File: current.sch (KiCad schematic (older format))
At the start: 42 parts, among them Q401 CJ2302, Q402 CJ2302, Q403 CJ2302, Q404 CJ2302, U401 MAX9919FASA+, U402 MAX9919FASA+, U403 MAX9919FASA+, U404 MAX9919FASA+, U405 MAX9919FASA+

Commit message: significant progress on placement, sch changes for adc routing
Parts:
- R403, R404, R407, R408, R409: footprint Resistors_SMD:R_1206 -> tm-kicad-lib:SMD-0805-R

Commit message: usb refactor on sch and pcb, mechanical constraints on bcp
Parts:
- U401, U402, U403, U404, U405: footprint SMD_Packages:SOIC-8-N -> tm-kicad-lib:SOIC-8-N-1EP

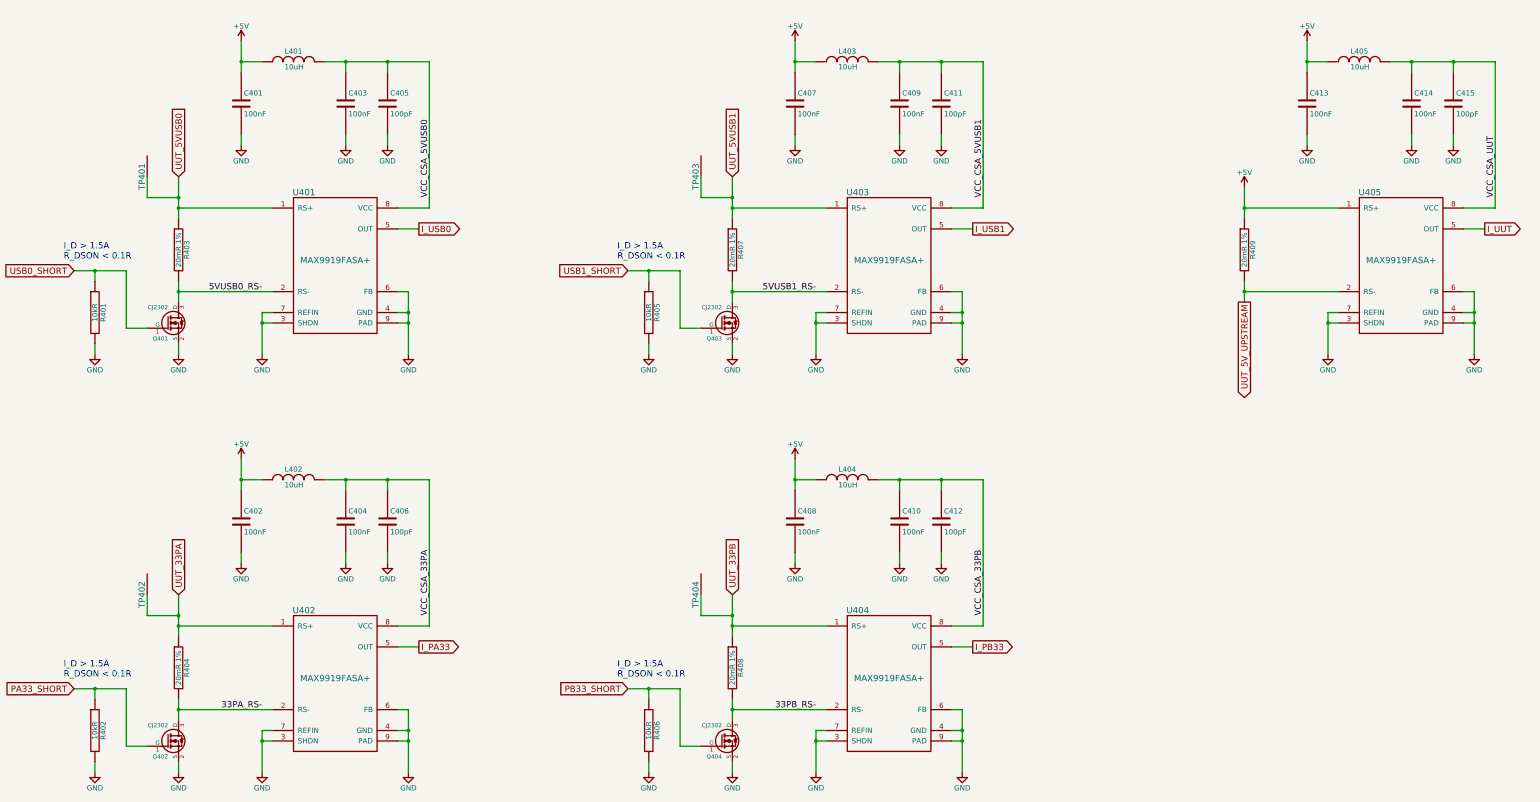
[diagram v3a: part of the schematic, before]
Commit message: consolidated csa power, removed drill map text
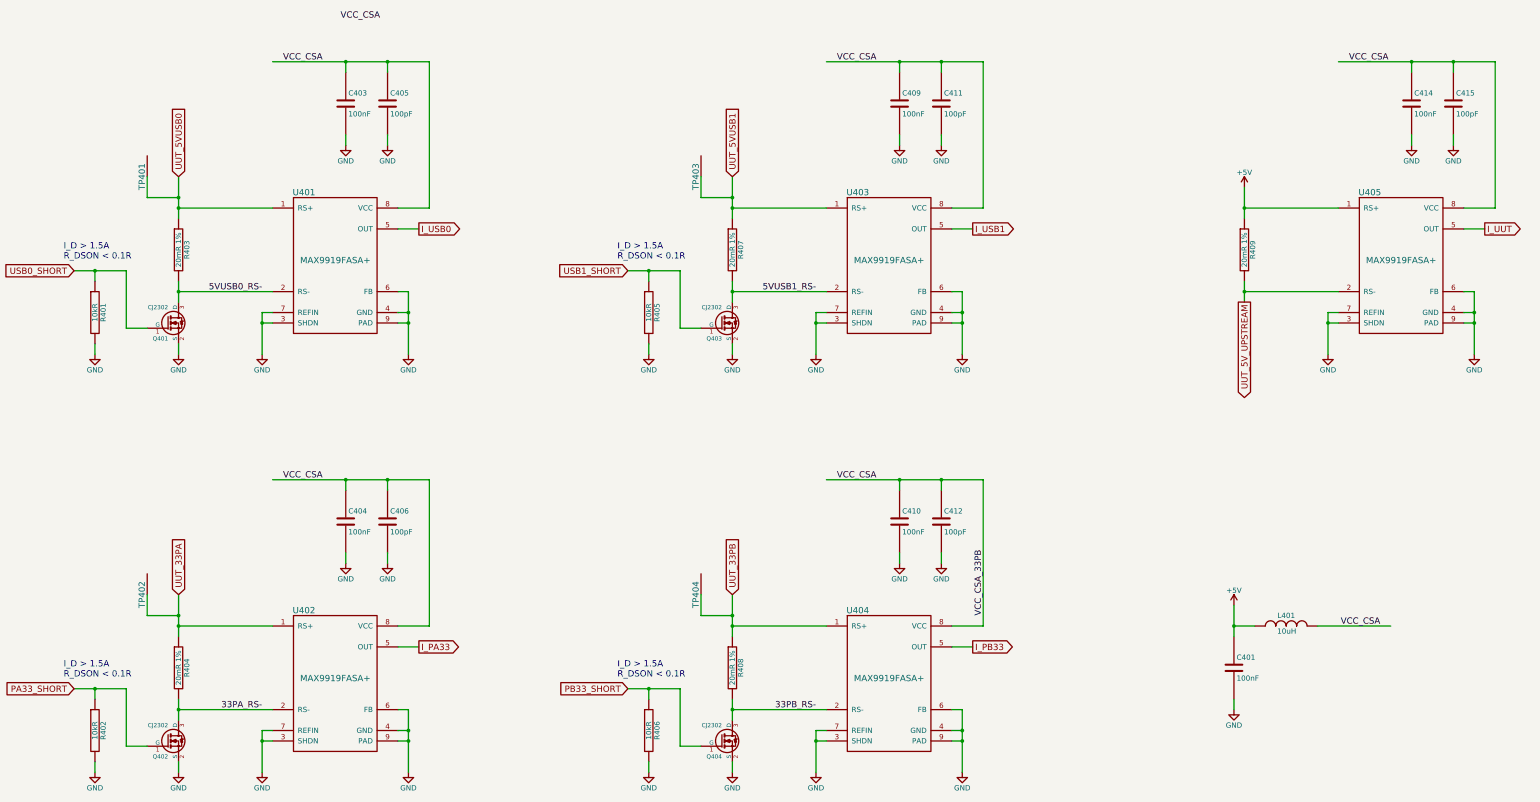
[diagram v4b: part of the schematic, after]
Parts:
- removed C402, C407, C408, C413: 100nF, tm-kicad-lib:SMD-0402-C, symbol TM_C
- removed L402, L403, L404, L405: 10uH, tm-kicad-lib:SMD-0603-R, symbol TM_L
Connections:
- net labels added: VCC_CSA
- net labels removed: VCC_CSA_33PA, VCC_CSA_5VUSB0, VCC_CSA_5VUSB1, VCC_CSA_UUT
- wire segments 142 -> 131
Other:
- moved on the sheet: C401, L401

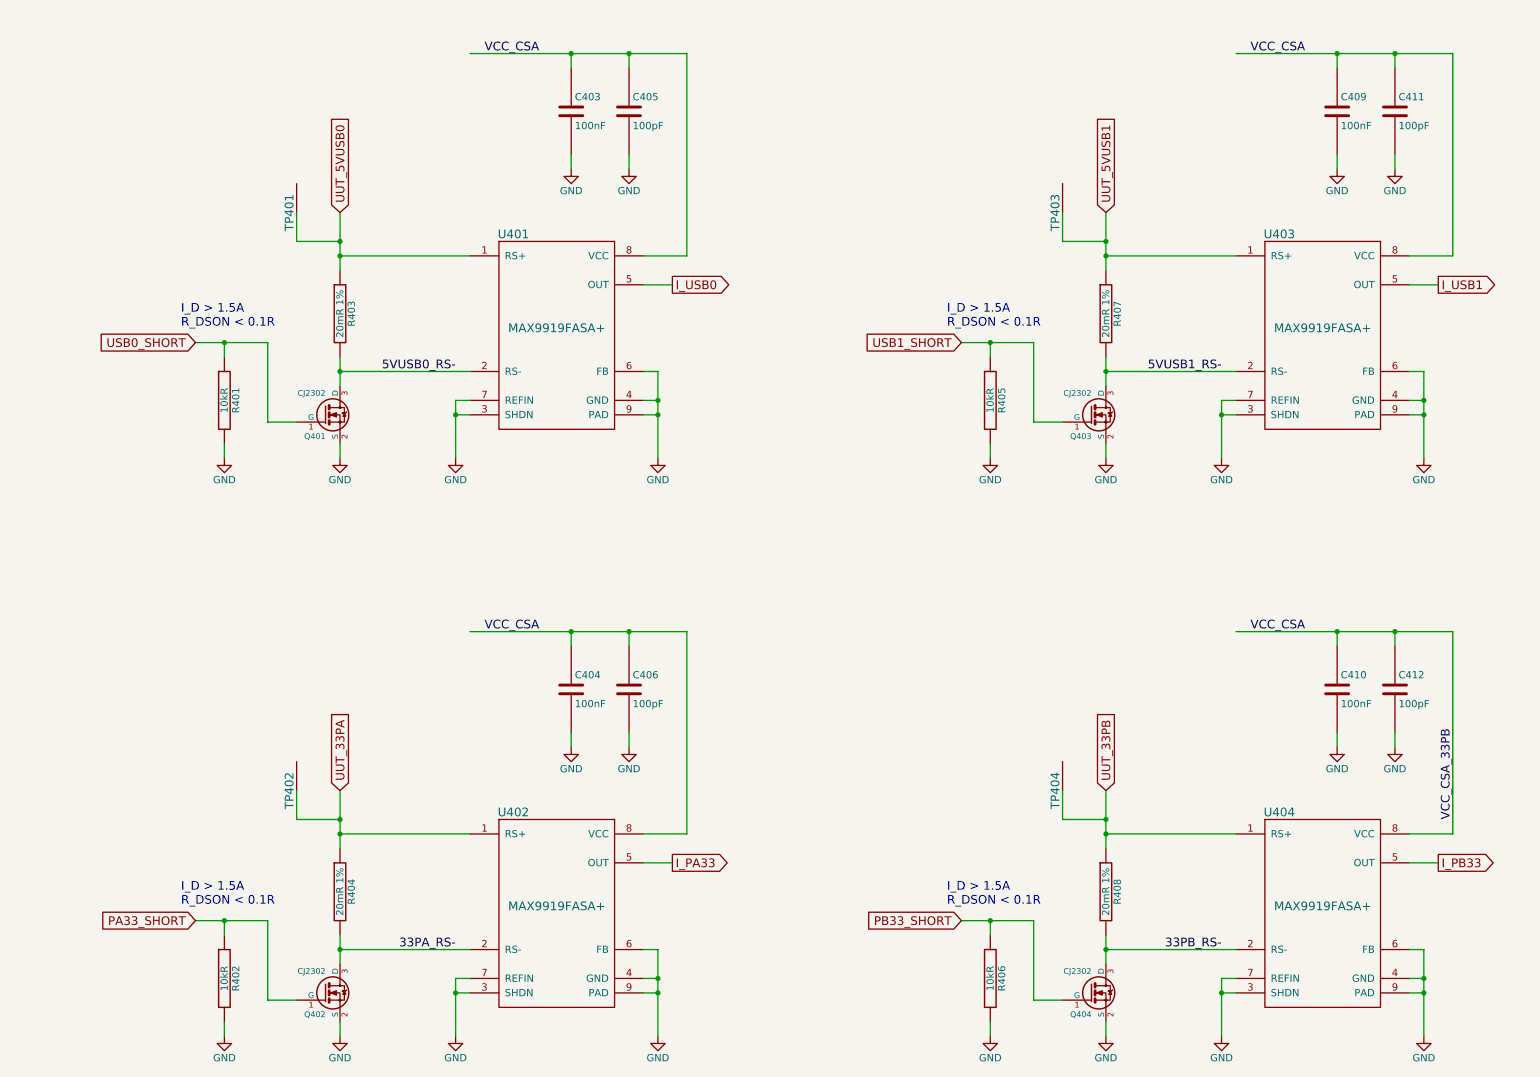
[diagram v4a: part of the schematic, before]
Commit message: mostly routed... time to go back and pin mux
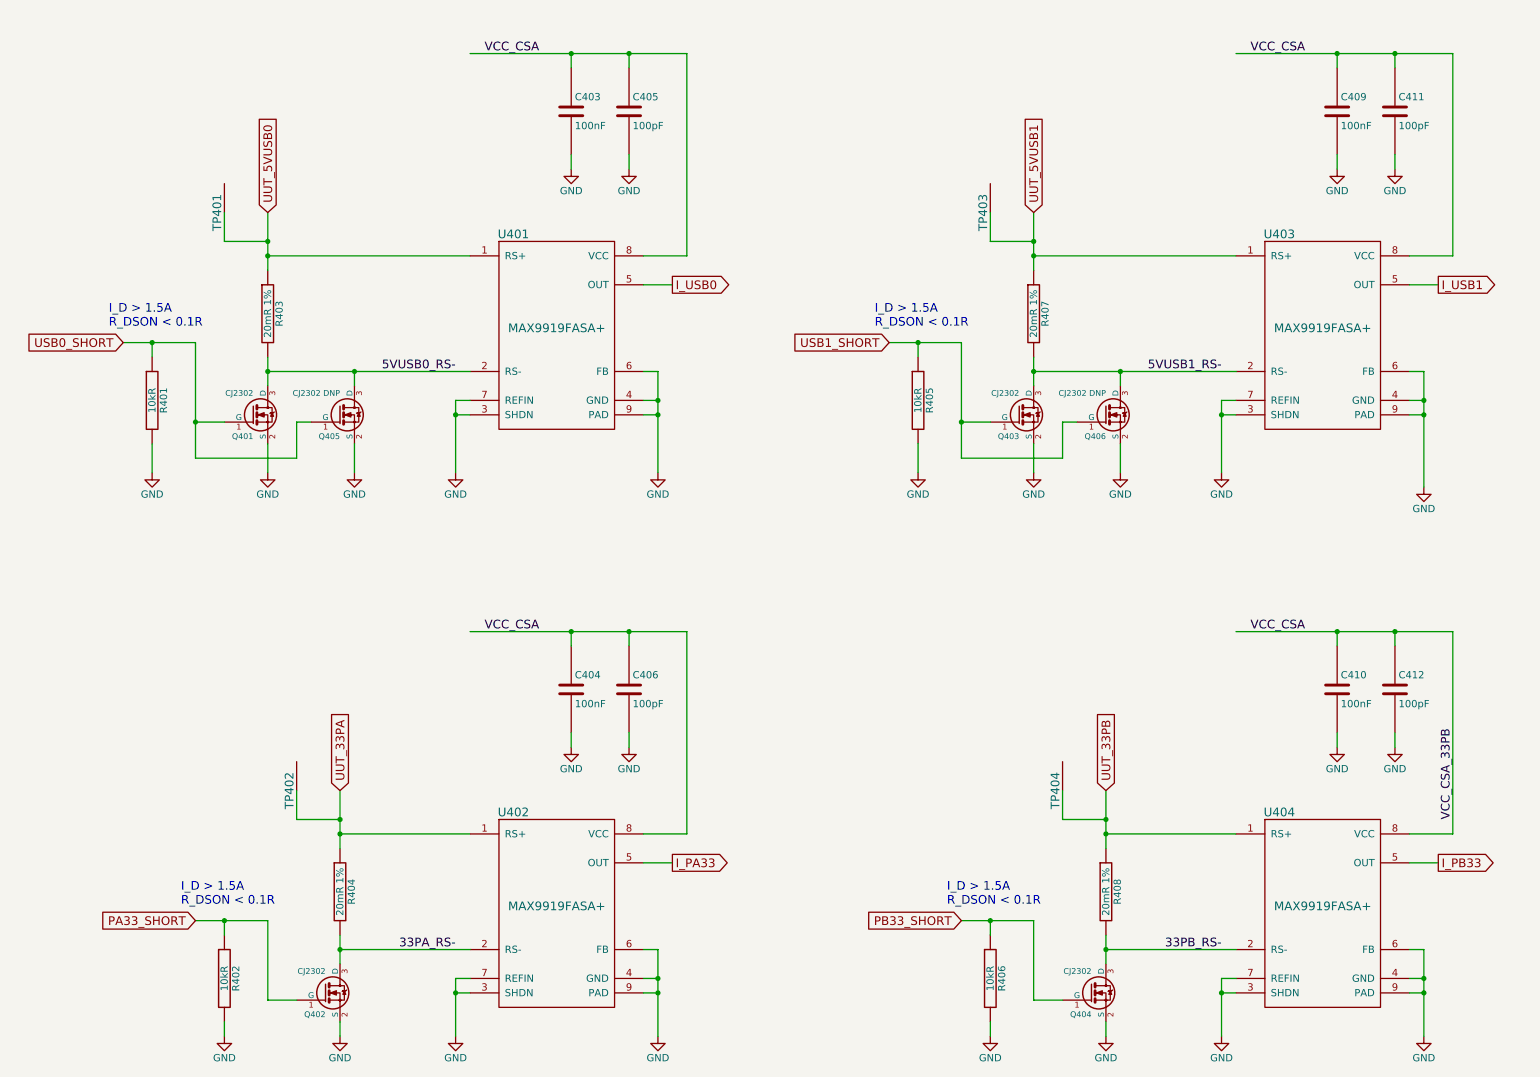
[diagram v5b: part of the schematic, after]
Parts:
- added Q405, Q406: CJ2302 DNP, Housings_SOT-23_SOT-143_TSOT-6:SOT-23, symbol nMOS
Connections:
- wire segments 131 -> 141
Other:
- moved on the sheet: Q401, Q403, R401, R403, R405, R407, TP401, TP403
